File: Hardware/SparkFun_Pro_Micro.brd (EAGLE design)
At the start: 17.8 x 33 mm, 105 parts, among them J2 Qwiic, U1 3.3V, U3 ATmega32U4, Y2 32MHz

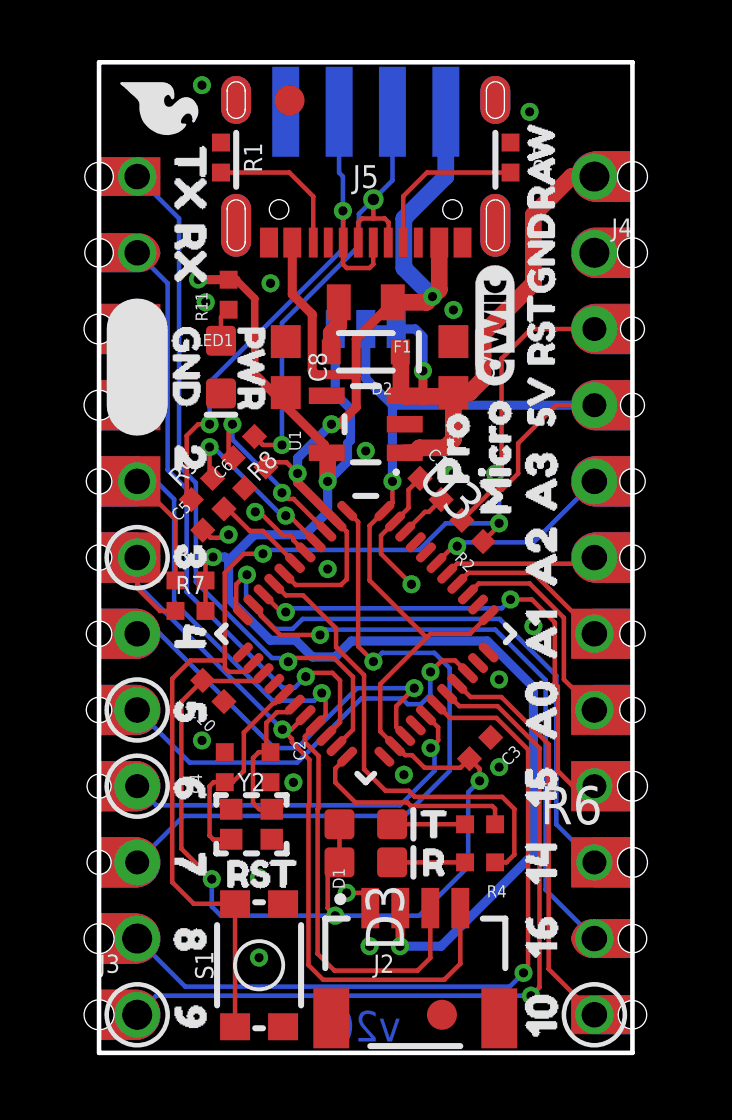
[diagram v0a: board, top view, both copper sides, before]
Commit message: Updates to Pro Micro and Frank
"Castellated" library '1x12CASTELLATED' and 'PRO_MICRO_C' footprints updated and 'PRO_MICRO_C' device updated.

Pro Micro C got uniform drill/ring sizing + added plated holes to outside in place of drills

Frank got 1U Keycap standard switch spacing and updated Pro Micro footprint.
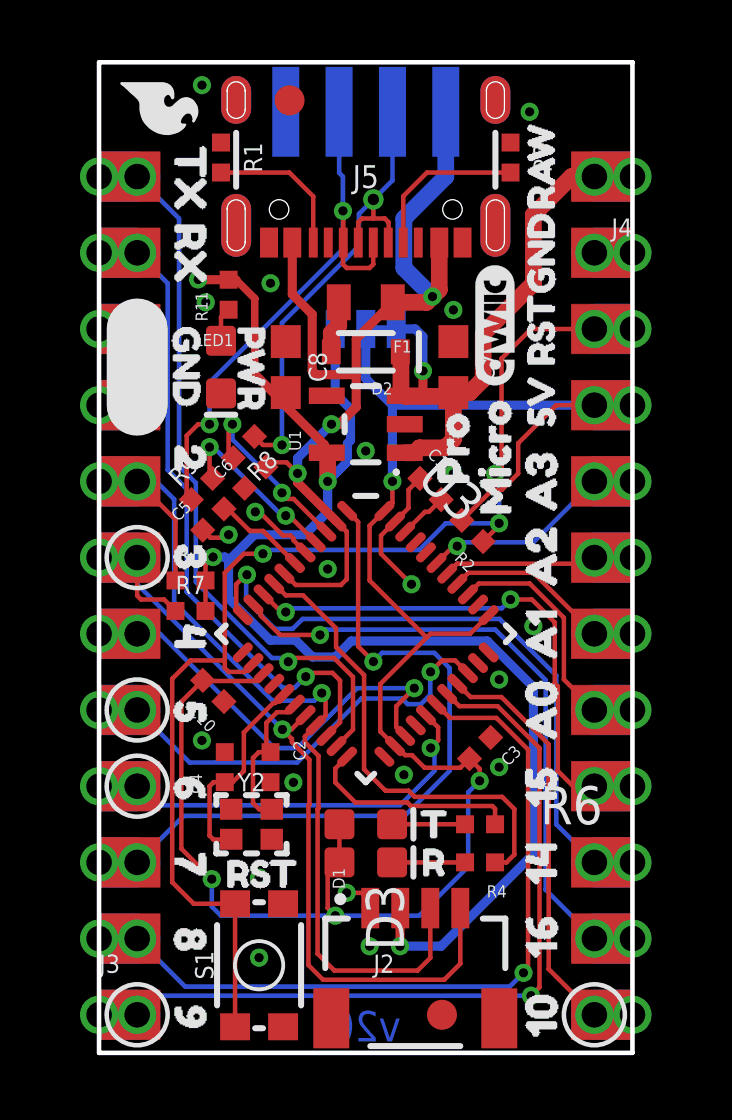
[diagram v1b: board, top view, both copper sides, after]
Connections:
- removed net N$3: J3.10
- net A0: now also J4.8B
- net A1: now also J4.7B
- net A2: now also J4.6B
- net A3: now also J4.5B
- net D10: now also J4.12B
- net D2/SDA: now also J3.8B
- net D3/SCL: now also J3.7B
- net D4: now also J3.6B
- net D5: now also J3.5B
- net D6: now also J3.4B
- net D7: now also J3.3B
- net D8: now also J3.2B
- net D9: now also J3.1B
- net GND: now also J3.10, J3.10B, J3.9B, J4.2B
- net MISO: now also J4.10B
- net MOSI: now also J4.11B
- net RAW: now also J4.1B
- net RESET: now also J4.3B
- net RXI: now also J3.11B
- net SCK: now also J4.9B
- net TXO: now also J3.12B
- net VCC: now also J4.4B
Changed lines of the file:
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@@
 <setting verticaltext="up"/>
 </settings>
-<grid distance="0.05" unitdist="inch" unit="inch" style="lines" multiple="1" display="yes" altdistance="0.0025" altunitdist="inch" altunit="inch"/>
+<grid distance="0.05" unitdist="inch" unit="inch" style="lines" multiple="1" display="yes" altdistance="0.005" altunitdist="inch" altunit="inch"/>
 <layers>
 <layer number="1" name="Top" color="4" fill="1" visible="yes" active="yes"/>
@@
 <contactref element="J5" pad="GND"/>
 <contactref element="J5" pad="GND2"/>
+<contactref element="J3" pad="9B"/>
+<contactref element="J4" pad="2B"/>
+<contactref element="J3" pad="10"/>
+<contactref element="J3" pad="10B"/>
 </signal>
 <signal name="AREF">
@@
 <wire x1="4.191" y1="13.081" x2="4.191" y2="12.827" width="0.1524" layer="1"/>
 <wire x1="3.048" y1="13.081" x2="4.191" y2="13.081" width="0.1524" layer="1"/>
+<contactref element="J4" pad="3B"/>
+<wire x1="16.51" y1="24.13" x2="17.78" y2="24.13" width="0" layer="19" extent="1-1"/>
 </signal>
 <signal name="SCK">
@@
 <wire x1="13.716" y1="15.113" x2="13.423946875" y2="14.820946875" width="0.1524" layer="16"/>
 <wire x1="13.423946875" y1="14.820946875" x2="6.35" y2="14.820946875" width="0.1524" layer="16"/>
+<contactref element="J4" pad="9B"/>
+<wire x1="16.51" y1="8.89" x2="17.78" y2="8.89" width="0" layer="19" extent="1-1"/>
 </signal>
 <signal name="N$38">
@@
 <contactref element="J4" pad="10"/>
 <wire x1="15.24" y1="7.62" x2="16.51" y2="6.35" width="0.1524" layer="16"/>
+<contactref element="J4" pad="10B"/>
+<wire x1="16.51" y1="6.35" x2="17.78" y2="6.35" width="0" layer="19" extent="1-1"/>
 </signal>
 <signal name="MOSI">
@@
 <contactref element="J4" pad="11"/>
 <wire x1="14.8844" y1="5.4356" x2="16.51" y2="3.81" width="0.1524" layer="16"/>
+<contactref element="J4" pad="11B"/>
+<wire x1="16.51" y1="3.81" x2="17.78" y2="3.81" width="0" layer="19" extent="1-1"/>
 </signal>
 <signal name="TXO">
@@
 <contactref element="J3" pad="12"/>
 <wire x1="2.667" y1="27.813" x2="1.27" y2="29.21" width="0.1524" layer="16"/>
+<contactref element="J3" pad="12B"/>
+<wire x1="1.27" y1="29.21" x2="0" y2="29.21" width="0" layer="19" extent="1-1"/>
 </signal>
 <signal name="VCC">
@@
 <contactref element="JP4" pad="2"/>
 <wire x1="8.89" y1="22.479" x2="8.89" y2="24.13" width="0.3048" layer="16"/>
+<contactref element="J4" pad="4B"/>
+<wire x1="16.51" y1="21.59" x2="17.78" y2="21.59" width="0" layer="19" extent="1-1"/>
 </signal>
 <signal name="RAW" class="1">
@@
 <wire x1="10.541" y1="24.13" x2="10.795" y2="23.876" width="0.3048" layer="16"/>
 <wire x1="10.795" y1="23.876" x2="10.795" y2="22.733" width="0.3048" layer="16"/>
+<contactref element="J4" pad="1B"/>
+<wire x1="16.51" y1="29.21" x2="17.78" y2="29.21" width="0" layer="19" extent="1-1"/>
 </signal>
 <signal name="D9">
@@
 <wire x1="14.6812" y1="10.16074375" x2="14.6812" y2="2.188" width="0.1524" layer="1"/>
 <wire x1="14.3982" y1="1.905" x2="1.905" y2="1.905" width="0.1524" layer="16"/>
+<contactref element="J3" pad="1B"/>
+<wire x1="0" y1="1.27" x2="1.27" y2="1.27" width="0" layer="19" extent="1-1"/>
 </signal>
 <signal name="D8">
@@
 <wire x1="14.30094375" y1="10.10994375" x2="14.30094375" y2="2.82014375" width="0.1524" layer="1"/>
 <wire x1="13.6906" y1="2.2098" x2="2.8702" y2="2.2098" width="0.1524" layer="16"/>
+<contactref element="J3" pad="2B"/>
+<wire x1="0" y1="3.81" x2="1.27" y2="3.81" width="0" layer="19" extent="1-1"/>
 </signal>
 <signal name="A3">
@@
 <wire x1="14.478" y1="17.018" x2="11.938" y2="17.018" width="0.1524" layer="16"/>
 <wire x1="14.478" y1="17.018" x2="16.51" y2="19.05" width="0.1524" layer="16"/>
+<contactref element="J4" pad="5B"/>
+<wire x1="16.51" y1="19.05" x2="17.78" y2="19.05" width="0" layer="19" extent="1-1"/>
 </signal>
 <signal name="A2">
@@
 <wire x1="16.3068" y1="16.3068" x2="16.51" y2="16.51" width="0.1524" layer="1"/>
 <wire x1="11.93390625" y1="16.3068" x2="16.3068" y2="16.3068" width="0.1524" layer="1"/>
+<contactref element="J4" pad="6B"/>
+<wire x1="16.51" y1="16.51" x2="17.78" y2="16.51" width="0" layer="19" extent="1-1"/>
 </signal>
 <signal name="A1">
@@
 <contactref element="J4" pad="7"/>
 <wire x1="14.478" y1="16.002" x2="16.51" y2="13.97" width="0.1524" layer="1"/>
+<contactref element="J4" pad="7B"/>
+<wire x1="16.51" y1="13.97" x2="17.78" y2="13.97" width="0" layer="19" extent="1-1"/>
 </signal>
 <signal name="A0">
@@
 <contactref element="J4" pad="8"/>
 <wire x1="15.494" y1="12.446" x2="16.51" y2="11.43" width="0.1524" layer="1"/>
+<contactref element="J4" pad="8B"/>
+<wire x1="16.51" y1="11.43" x2="17.78" y2="11.43" width="0" layer="19" extent="1-1"/>
 </signal>
 <signal name="D2/SDA">
@@
 <wire x1="2.548" y1="15.748" x2="2.548" y2="17.772" width="0.1524" layer="1"/>
 <wire x1="2.548" y1="17.772" x2="1.27" y2="19.05" width="0.1524" layer="1"/>
+<contactref element="J3" pad="8B"/>
+<wire x1="1.27" y1="19.05" x2="0" y2="19.05" width="0" layer="19" extent="1-1"/>
 </signal>
 <signal name="D3/SCL">
@@
 <wire x1="7.4676" y1="2.4384" x2="6.9796" y2="2.9264" width="0.1524" layer="1"/>
 <wire x1="11.50545625" y1="2.4384" x2="7.4676" y2="2.4384" width="0.1524" layer="1"/>
-<wire x1="2.548" y1="14.732" x2="2.032" y2="14.732" width="0.1524" layer="1"/>
-<wire x1="2.032" y1="14.732" x2="1.27" y2="15.494" width="0.1524" layer="1"/>
-<wire x1="1.27" y1="15.494" x2="1.27" y2="16.51" width="0.1524" layer="1"/>
+<wire x1="2.548" y1="14.732" x2="2.167" y2="15.113" width="0.1524" layer="1"/>
+<wire x1="2.167" y1="15.113" x2="1.397" y2="15.113" width="0.1524" layer="1"/>
+<wire x1="1.397" y1="15.113" x2="1.27" y2="15.24" width="0.1524" layer="1"/>
+<wire x1="1.27" y1="15.24" x2="1.27" y2="16.51" width="0.1524" layer="1"/>
+<contactref element="J3" pad="7B"/>
+<wire x1="1.27" y1="16.51" x2="0" y2="16.51" width="0" layer="19" extent="1-1"/>
 </signal>
 <signal name="D4">
@@
 <contactref element="J3" pad="6"/>
 <wire x1="1.27" y1="13.97" x2="2.032" y2="13.97" width="0.1524" layer="16"/>
+<contactref element="J3" pad="6B"/>
+<wire x1="0" y1="13.97" x2="1.27" y2="13.97" width="0" layer="19" extent="1-1"/>
 </signal>
 <signal name="D5">
@@
 <wire x1="8.7376" y1="11.811" x2="6.604" y2="9.6774" width="0.1524" layer="16"/>
 <wire x1="10.09719375" y1="11.811" x2="8.7376" y2="11.811" width="0.1524" layer="16"/>
+<contactref element="J3" pad="5B"/>
+<wire x1="0" y1="11.43" x2="1.27" y2="11.43" width="0" layer="19" extent="1-1"/>
 </signal>
 <signal name="D6">
@@
 <contactref element="J3" pad="4"/>
 <wire x1="1.27" y1="8.89" x2="1.905" y2="8.255" width="0.1524" layer="16"/>
+<contactref element="J3" pad="4B"/>
+<wire x1="0" y1="8.89" x2="1.27" y2="8.89" width="0" layer="19" extent="1-1"/>
 </signal>
 <signal name="D7">
@@
 <wire x1="2.8194" y1="7.8994" x2="1.27" y2="6.35" width="0.1524" layer="16"/>
 <wire x1="11.684" y1="9.398" x2="10.1854" y2="7.8994" width="0.1524" layer="16"/>
+<contactref element="J3" pad="3B"/>
+<wire x1="0" y1="6.35" x2="1.27" y2="6.35" width="0" layer="19" extent="1-1"/>
 </signal>
 <signal name="D10">
@@
 <contactref element="J4" pad="12"/>
 <wire x1="14.986" y1="2.794" x2="16.51" y2="1.27" width="0.1524" layer="1"/>
+<contactref element="J4" pad="12B"/>
+<wire x1="16.51" y1="1.27" x2="17.78" y2="1.27" width="0" layer="19" extent="1-1"/>
 </signal>
 <signal name="N$1">
@@
 <contactref element="J3" pad="11"/>
 <wire x1="2.286" y1="25.654" x2="1.27" y2="26.67" width="0.1524" layer="16"/>
+<contactref element="J3" pad="11B"/>
+<wire x1="1.27" y1="26.67" x2="0" y2="26.67" width="0" layer="19" extent="1-1"/>
 </signal>
 <signal name="D-">
@@
 <wire x1="5.460996875" y1="17.399" x2="5.02510625" y2="17.399" width="0.1524" layer="1"/>
 </signal>
-<signal name="N$3">
-<contactref element="J3" pad="10"/>
-</signal>
 <signal name="3.3V">

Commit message: Red boards ordered
Modify castellated 1x12 to larger diameter plated castellated holes. Panelize with route-out around castellated edges. Scoot Qwiic connector in to use that side of the board as the tab.
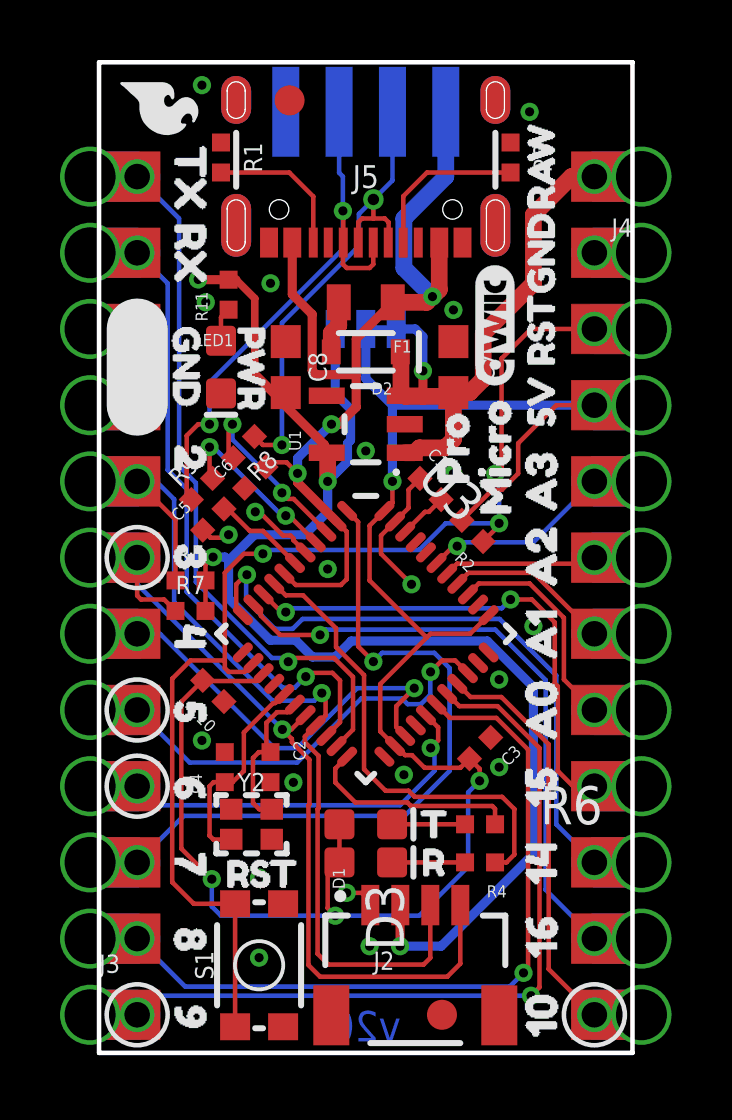
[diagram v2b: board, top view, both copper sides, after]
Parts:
- removed U$20: (no value), SparkFun-Aesthetics:PRODUCTION_INSTRUCTIONS
- added LOGO5: SPECIAL_INSTRUCTIONS-ORDERING, SparkFun-Aesthetics:ORDERING_INSTRUCTIONS
- moved FRAME1 37.6 mm to (20.3, -8.89)
- moved J2 0.10 mm to (10.5, 4.93)
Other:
- board text added: "N Seidle"
- board text removed: "N. Seidle"

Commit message: Udpate xtal to 16MHz
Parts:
- Y2: value 32MHz -> 16MHz
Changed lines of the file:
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@@
 <?xml version="1.0" encoding="utf-8"?>
 <!DOCTYPE eagle SYSTEM "eagle.dtd">
-<eagle version="9.5.1">
+<eagle version="9.5.2">
 <drawing>
 <settings>
@@
 </element>
 <element name="LOGO1" library="SparkFun-Aesthetics" package="SFE_LOGO_NAME_FLAME_.1" value="SFE_LOGO_NAME_FLAME.1_INCH" x="8.89" y="16.51" smashed="yes" rot="MR90"/>
-<element name="Y2" library="SparkFun-Clocks" package="CRYSTAL-SMD-2.0X1.6MM" value="32MHz" x="5.08" y="7.62" smashed="yes">
+<element name="Y2" library="SparkFun-Clocks" package="CRYSTAL-SMD-2.0X1.6MM" value="16MHz" x="5.08" y="7.62" smashed="yes">
 <attribute name="NAME" x="5.079996875" y="8.719996875" size="0.6096" layer="25" ratio="20" align="bottom-center"/>
-<attribute name="PROD_ID" value="XTAL-13459" x="5.08" y="7.62" size="1.778" layer="27" font="vector" ratio="15" display="off"/>
-<attribute name="VALUE" x="5.079996875" y="6.52" size="0.6096" layer="27" ratio="20" align="top-center"/>
+<attribute name="PROD_ID" value="XTAL-14681" x="5.08" y="7.62" size="1.778" layer="27" font="vector" ratio="15" display="off"/>
+<attribute name="VALUE" value="16MHz" x="5.079996875" y="6.52" size="0.6096" layer="27" ratio="20" align="top-center"/>
 </element>
 <element name="J2" library="SparkFun-Connectors" package="JST04_1MM_RA" value="Qwiic" x="10.541" y="4.926" smashed="yes">
